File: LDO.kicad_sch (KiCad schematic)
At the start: 5 parts, among them U4 MCP1826S

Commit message: AGND
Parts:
- renumbered C37 to C31, C38 to C32, U4 to U5
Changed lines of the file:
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@@
 		(dnp no)
 		(fields_autoplaced yes)
-		(property "Reference" "C38"
+		(property "Reference" "C32"
 			(at 168.275 68.5735 0)
 			(show_name no)
@@
 			(project "PS-PrechargeBoard"
 				(path "/74d17fe6-68d4-4bd7-954a-e2bbb58b1f1e/2ca150cf-fbe5-4d5b-a7dc-f2dc5c6024d0/948d6922-1fd9-4543-b1e5-414190ab0379"
-					(reference "C38")
+					(reference "C32")
 					(unit 1)
 				)
@@
 		(dnp no)
 		(fields_autoplaced yes)
-		(property "Reference" "U4"
+		(property "Reference" "U5"
 			(at 152.4 56.515 0)
 			(show_name no)
@@
 			(project "PS-PrechargeBoard"
 				(path "/74d17fe6-68d4-4bd7-954a-e2bbb58b1f1e/2ca150cf-fbe5-4d5b-a7dc-f2dc5c6024d0/948d6922-1fd9-4543-b1e5-414190ab0379"
-					(reference "U4")
+					(reference "U5")
 					(unit 1)
 				)
@@
 		(dnp no)
 		(fields_autoplaced yes)
-		(property "Reference" "C37"
+		(property "Reference" "C31"
 			(at 142.875 68.5735 0)
 			(show_name no)
@@
 			(project "PS-PrechargeBoard"
 				(path "/74d17fe6-68d4-4bd7-954a-e2bbb58b1f1e/2ca150cf-fbe5-4d5b-a7dc-f2dc5c6024d0/948d6922-1fd9-4543-b1e5-414190ab0379"
-					(reference "C37")
+					(reference "C31")
 					(unit 1)
 				)

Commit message: isolated precharge from fuse
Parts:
- renumbered C31 to C33, C32 to C34
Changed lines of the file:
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@@
 		(dnp no)
 		(fields_autoplaced yes)
-		(property "Reference" "C32"
+		(property "Reference" "C34"
 			(at 168.275 68.5735 0)
 			(show_name no)
@@
 			(project "PS-PrechargeBoard"
 				(path "/74d17fe6-68d4-4bd7-954a-e2bbb58b1f1e/2ca150cf-fbe5-4d5b-a7dc-f2dc5c6024d0/948d6922-1fd9-4543-b1e5-414190ab0379"
-					(reference "C32")
+					(reference "C34")
 					(unit 1)
 				)
@@
 		(dnp no)
 		(fields_autoplaced yes)
-		(property "Reference" "C31"
+		(property "Reference" "C33"
 			(at 142.875 68.5735 0)
 			(show_name no)
@@
 			(project "PS-PrechargeBoard"
 				(path "/74d17fe6-68d4-4bd7-954a-e2bbb58b1f1e/2ca150cf-fbe5-4d5b-a7dc-f2dc5c6024d0/948d6922-1fd9-4543-b1e5-414190ab0379"
-					(reference "C31")
+					(reference "C33")
 					(unit 1)
 				)

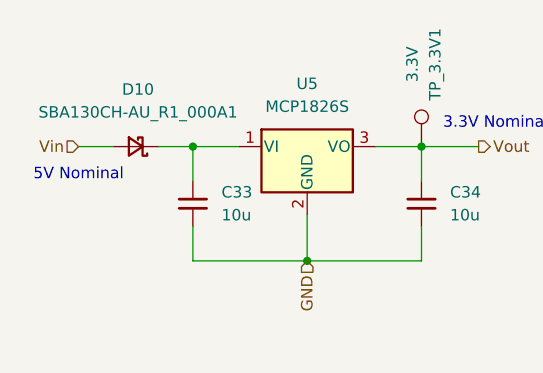
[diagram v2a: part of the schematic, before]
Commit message: voltage sensor cleanup
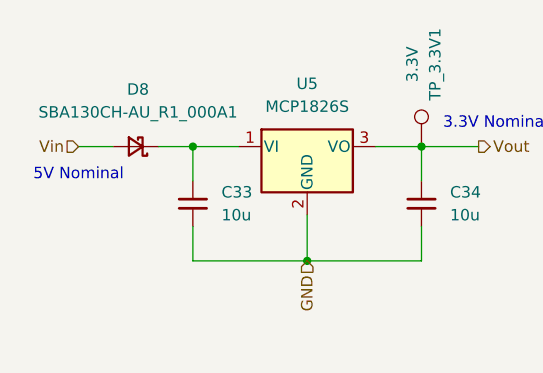
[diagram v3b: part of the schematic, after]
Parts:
- renumbered D10 to D8
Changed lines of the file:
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@@
 		(dnp no)
 		(fields_autoplaced yes)
-		(property "Reference" "D10"
+		(property "Reference" "D8"
 			(at 133.604 57.15 0)
 			(show_name no)
@@
 			(project "PS-PrechargeBoard"
 				(path "/74d17fe6-68d4-4bd7-954a-e2bbb58b1f1e/2ca150cf-fbe5-4d5b-a7dc-f2dc5c6024d0/948d6922-1fd9-4543-b1e5-414190ab0379"
-					(reference "D10")
+					(reference "D8")
 					(unit 1)
 				)

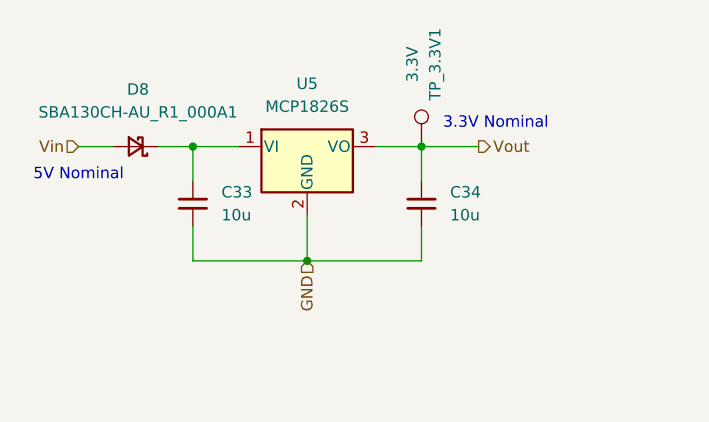
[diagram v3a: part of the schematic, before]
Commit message: updated usb-c connector
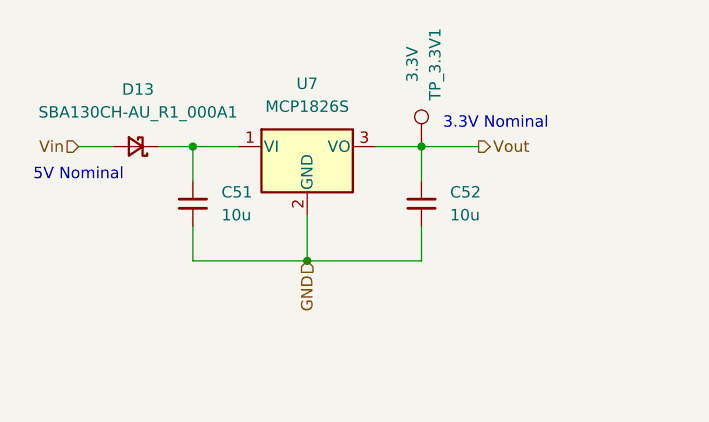
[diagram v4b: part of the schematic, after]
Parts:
- renumbered C33 to C51, C34 to C52, D8 to D13, U5 to U7
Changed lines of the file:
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@@
 		(dnp no)
 		(fields_autoplaced yes)
-		(property "Reference" "C34"
+		(property "Reference" "C52"
 			(at 168.275 68.5735 0)
 			(show_name no)
@@
 			(project "PS-PrechargeBoard"
 				(path "/74d17fe6-68d4-4bd7-954a-e2bbb58b1f1e/2ca150cf-fbe5-4d5b-a7dc-f2dc5c6024d0/948d6922-1fd9-4543-b1e5-414190ab0379"
-					(reference "C34")
+					(reference "C52")
 					(unit 1)
 				)
@@
 		(dnp no)
 		(fields_autoplaced yes)
-		(property "Reference" "U5"
+		(property "Reference" "U7"
 			(at 152.4 56.515 0)
 			(show_name no)
@@
 			(project "PS-PrechargeBoard"
 				(path "/74d17fe6-68d4-4bd7-954a-e2bbb58b1f1e/2ca150cf-fbe5-4d5b-a7dc-f2dc5c6024d0/948d6922-1fd9-4543-b1e5-414190ab0379"
-					(reference "U5")
+					(reference "U7")
 					(unit 1)
 				)
@@
 		(dnp no)
 		(fields_autoplaced yes)
-		(property "Reference" "D8"
+		(property "Reference" "D13"
 			(at 133.604 57.15 0)
 			(show_name no)
@@
 			(project "PS-PrechargeBoard"
 				(path "/74d17fe6-68d4-4bd7-954a-e2bbb58b1f1e/2ca150cf-fbe5-4d5b-a7dc-f2dc5c6024d0/948d6922-1fd9-4543-b1e5-414190ab0379"
-					(reference "D8")
+					(reference "D13")
 					(unit 1)
 				)
@@
 		(dnp no)
 		(fields_autoplaced yes)
-		(property "Reference" "C33"
+		(property "Reference" "C51"
 			(at 142.875 68.5735 0)
 			(show_name no)
@@
 			(project "PS-PrechargeBoard"
 				(path "/74d17fe6-68d4-4bd7-954a-e2bbb58b1f1e/2ca150cf-fbe5-4d5b-a7dc-f2dc5c6024d0/948d6922-1fd9-4543-b1e5-414190ab0379"
-					(reference "C33")
+					(reference "C51")
 					(unit 1)
 				)

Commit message: fixed hv placement
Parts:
- TP_3.3V1: footprint TestPoint:TestPoint_Loop_D1.80mm_Drill1.0mm_Beaded -> TestPoint:TestPoint_THTPad_D3.0mm_Drill1.5mm
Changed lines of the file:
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@@
 			)
 		)
-		(property "Footprint" "TestPoint:TestPoint_Loop_D1.80mm_Drill1.0mm_Beaded"
+		(property "Footprint" "TestPoint:TestPoint_THTPad_D3.0mm_Drill1.5mm"
 			(at 170.18 63.5 0)
 			(hide yes)
